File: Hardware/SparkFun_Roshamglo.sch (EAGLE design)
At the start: 41 parts, among them IC1 ATTINY84A, J1 R_Ext, J2 USBPCB, Q1 600mA/40V, U1 IR-Receiver, U3 AP2112K-3.3V

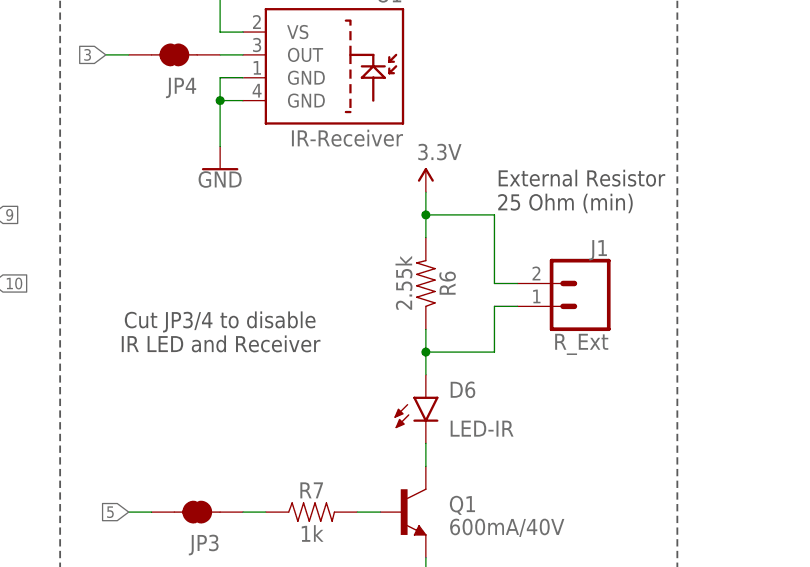
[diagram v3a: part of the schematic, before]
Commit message: v10 - replaced 2.55k resistor with 2.2k
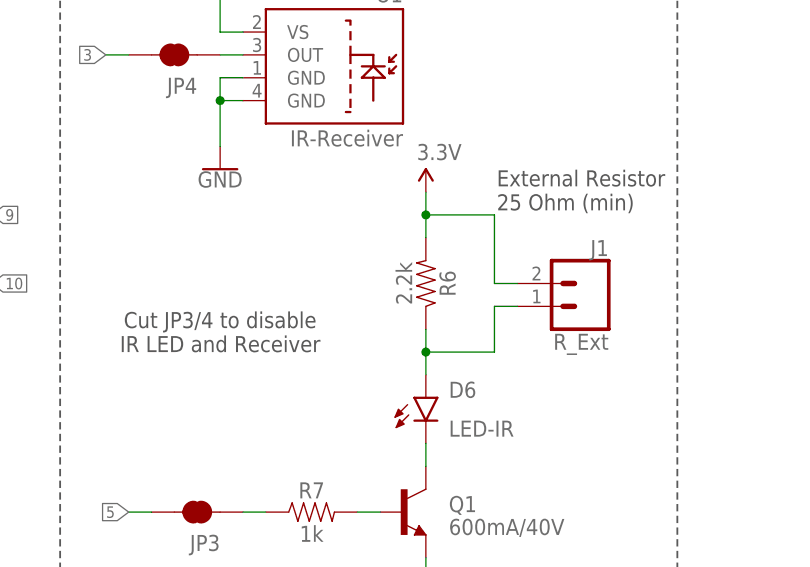
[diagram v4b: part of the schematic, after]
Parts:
- R6: value 2.55k -> 2.2k; device SparkFun-Resistors:2.55KOHM-0603-1/10W-1% -> SparkFun-Resistors:2.2KOHM-0603-1/10W-1%
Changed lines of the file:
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@@
 <grid distance="0.1" unitdist="inch" unit="inch" style="lines" multiple="1" display="no" altdistance="0.01" altunitdist="inch" altunit="inch"/>
 <layers>
-<layer number="1" name="Top" color="4" fill="1" visible="yes" active="no"/>
-<layer number="2" name="Route2" color="1" fill="3" visible="yes" active="no"/>
-<layer number="3" name="Route3" color="4" fill="3" visible="yes" active="no"/>
-<layer number="4" name="Route4" color="1" fill="4" visible="yes" active="no"/>
-<layer number="5" name="Route5" color="4" fill="4" visible="yes" active="no"/>
-<layer number="6" name="Route6" color="1" fill="8" visible="yes" active="no"/>
-<layer number="7" name="Route7" color="4" fill="8" visible="yes" active="no"/>
-<layer number="8" name="Route8" color="1" fill="2" visible="yes" active="no"/>
-<layer number="9" name="Route9" color="4" fill="2" visible="yes" active="no"/>
-<layer number="10" name="Route10" color="1" fill="7" visible="yes" active="no"/>
-<layer number="11" name="Route11" color="4" fill="7" visible="yes" active="no"/>
-<layer number="12" name="Route12" color="1" fill="5" visible="yes" active="no"/>
-<layer number="13" name="Route13" color="4" fill="5" visible="yes" active="no"/>
-<layer number="14" name="Route14" color="1" fill="6" visible="yes" active="no"/>
-<layer number="15" name="Route15" color="4" fill="6" visible="yes" active="no"/>
-<layer number="16" name="Bottom" color="1" fill="1" visible="yes" active="no"/>
-<layer number="17" name="Pads" color="2" fill="1" visible="yes" active="no"/>
-<layer number="18" name="Vias" color="2" fill="1" visible="yes" active="no"/>
-<layer number="19" name="Unrouted" color="6" fill="1" visible="yes" active="no"/>
-<layer number="20" name="Dimension" color="15" fill="1" visible="yes" active="no"/>
-<layer number="21" name="tPlace" color="16" fill="1" visible="yes" active="no"/>
-<layer number="22" name="bPlace" color="14" fill="1" visible="yes" active="no"/>
-<layer number="23" name="tOrigins" color="15" fill="1" visible="yes" active="no"/>
-<layer number="24" name="bOrigins" color="15" fill="1" visible="yes" active="no"/>
-<layer number="25" name="tNames" color="7" fill="1" visible="yes" active="no"/>
-<layer number="26" name="bNames" color="7" fill="1" visible="yes" active="no"/>
-<layer number="27" name="tValues" color="7" fill="1" visible="yes" active="no"/>
-<layer number="28" name="bValues" color="7" fill="1" visible="yes" active="no"/>
+<layer number="1" name="Top" color="4" fill="1" visible="no" active="no"/>
+<layer number="2" name="Route2" color="1" fill="3" visible="no" active="no"/>
+<layer number="3" name="Route3" color="4" fill="3" visible="no" active="no"/>
+<layer number="4" name="Route4" color="1" fill="4" visible="no" active="no"/>
+<layer number="5" name="Route5" color="4" fill="4" visible="no" active="no"/>
+<layer number="6" name="Route6" color="1" fill="8" visible="no" active="no"/>
+<layer number="7" name="Route7" color="4" fill="8" visible="no" active="no"/>
+<layer number="8" name="Route8" color="1" fill="2" visible="no" active="no"/>
+<layer number="9" name="Route9" color="4" fill="2" visible="no" active="no"/>
+<layer number="10" name="Route10" color="1" fill="7" visible="no" active="no"/>
+<layer number="11" name="Route11" color="4" fill="7" visible="no" active="no"/>
+<layer number="12" name="Route12" color="1" fill="5" visible="no" active="no"/>
+<layer number="13" name="Route13" color="4" fill="5" visible="no" active="no"/>
+<layer number="14" name="Route14" color="1" fill="6" visible="no" active="no"/>
+<layer number="15" name="Route15" color="4" fill="6" visible="no" active="no"/>
+<layer number="16" name="Bottom" color="1" fill="1" visible="no" active="no"/>
+<layer number="17" name="Pads" color="2" fill="1" visible="no" active="no"/>
+<layer number="18" name="Vias" color="2" fill="1" visible="no" active="no"/>
+<layer number="19" name="Unrouted" color="6" fill="1" visible="no" active="no"/>
+<layer number="20" name="Dimension" color="15" fill="1" visible="no" active="no"/>
+<layer number="21" name="tPlace" color="16" fill="1" visible="no" active="no"/>
+<layer number="22" name="bPlace" color="14" fill="1" visible="no" active="no"/>
+<layer number="23" name="tOrigins" color="15" fill="1" visible="no" active="no"/>
+<layer number="24" name="bOrigins" color="15" fill="1" visible="no" active="no"/>
+<layer number="25" name="tNames" color="7" fill="1" visible="no" active="no"/>
+<layer number="26" name="bNames" color="7" fill="1" visible="no" active="no"/>
+<layer number="27" name="tValues" color="7" fill="1" visible="no" active="no"/>
+<layer number="28" name="bValues" color="7" fill="1" visible="no" active="no"/>
 <layer number="29" name="tStop" color="7" fill="3" visible="no" active="no"/>
 <layer number="30" name="bStop" color="7" fill="6" visible="no" active="no"/>
@@
 <layer number="35" name="tGlue" color="7" fill="4" visible="no" active="no"/>
 <layer number="36" name="bGlue" color="7" fill="5" visible="no" active="no"/>
-<layer number="37" name="tTest" color="7" fill="1" visible="yes" active="no"/>
-<layer number="38" name="bTest" color="7" fill="1" visible="yes" active="no"/>
+<layer number="37" name="tTest" color="7" fill="1" visible="no" active="no"/>
+<layer number="38" name="bTest" color="7" fill="1" visible="no" active="no"/>
 <layer number="39" name="tKeepout" color="4" fill="11" visible="no" active="no"/>
 <layer number="40" name="bKeepout" color="1" fill="11" visible="no" active="no"/>
@@
 <layer number="44" name="Drills" color="7" fill="1" visible="no" active="no"/>
 <layer number="45" name="Holes" color="7" fill="1" visible="no" active="no"/>
-<layer number="46" name="Milling" color="3" fill="1" visible="yes" active="no"/>
-<layer number="47" name="Measures" color="7" fill="1" visible="yes" active="no"/>
-<layer number="48" name="Document" color="7" fill="1" visible="yes" active="no"/>
-<layer number="49" name="Reference" color="7" fill="1" visible="yes" active="no"/>
-<layer number="50" name="dxf" color="7" fill="1" visible="yes" active="no"/>
-<layer number="51" name="tDocu" color="6" fill="1" visible="yes" active="no"/>
-<layer number="52" name="bDocu" color="7" fill="1" visible="yes" active="no"/>
-<layer number="53" name="tGND_GNDA" color="7" fill="9" visible="yes" active="no"/>
-<layer number="54" name="bGND_GNDA" color="1" fill="9" visible="yes" active="no"/>
-<layer number="56" name="wert" color="7" fill="1" visible="yes" active="no"/>
-<layer number="57" name="tCAD" color="7" fill="1" visible="yes" active="no"/>
-<layer number="59" name="tCarbon" color="7" fill="1" visible="yes" active="no"/>
-<layer number="60" name="bCarbon" color="7" fill="1" visible="yes" active="no"/>
+<layer number="46" name="Milling" color="3" fill="1" visible="no" active="no"/>
+<layer number="47" name="Measures" color="7" fill="1" visible="no" active="no"/>
+<layer number="48" name="Document" color="7" fill="1" visible="no" active="no"/>
+<layer number="49" name="Reference" color="7" fill="1" visible="no" active="no"/>
+<layer number="50" name="dxf" color="7" fill="1" visible="no" active="no"/>
+<layer number="51" name="tDocu" color="6" fill="1" visible="no" active="no"/>
+<layer number="52" name="bDocu" color="7" fill="1" visible="no" active="no"/>
+<layer number="53" name="tGND_GNDA" color="7" fill="9" visible="no" active="no"/>
+<layer number="54" name="bGND_GNDA" color="1" fill="9" visible="no" active="no"/>
+<layer number="56" name="wert" color="7" fill="1" visible="no" active="no"/>
+<layer number="57" name="tCAD" color="7" fill="1" visible="no" active="no"/>
+<layer number="59" name="tCarbon" color="7" fill="1" visible="no" active="no"/>
+<layer number="60" name="bCarbon" color="7" fill="1" visible="no" active="no"/>
 <layer number="90" name="Modules" color="5" fill="1" visible="yes" active="yes"/>
 <layer number="91" name="Nets" color="2" fill="1" visible="yes" active="yes"/>
@@
 <part name="SUPPLY9" library="SparkFun-Aesthetics" deviceset="3.3V" device=""/>
 <part name="SUPPLY13" library="SparkFun-PowerSymbols" deviceset="VIN" device=""/>
-<part name="R6" library="SparkFun-Resistors" deviceset="2.55KOHM" device="-0603-1/10W-1%" value="2.55k"/>
+<part name="R6" library="SparkFun-Resistors" deviceset="2.2KOHM" device="-0603-1/10W-1%" value="2.2k"/>
 <part name="FD1" library="SparkFun-Aesthetics" deviceset="FIDUCIAL" device="UFIDUCIAL"/>
 <part name="FD2" library="SparkFun-Aesthetics" deviceset="FIDUCIAL" device="UFIDUCIAL"/>

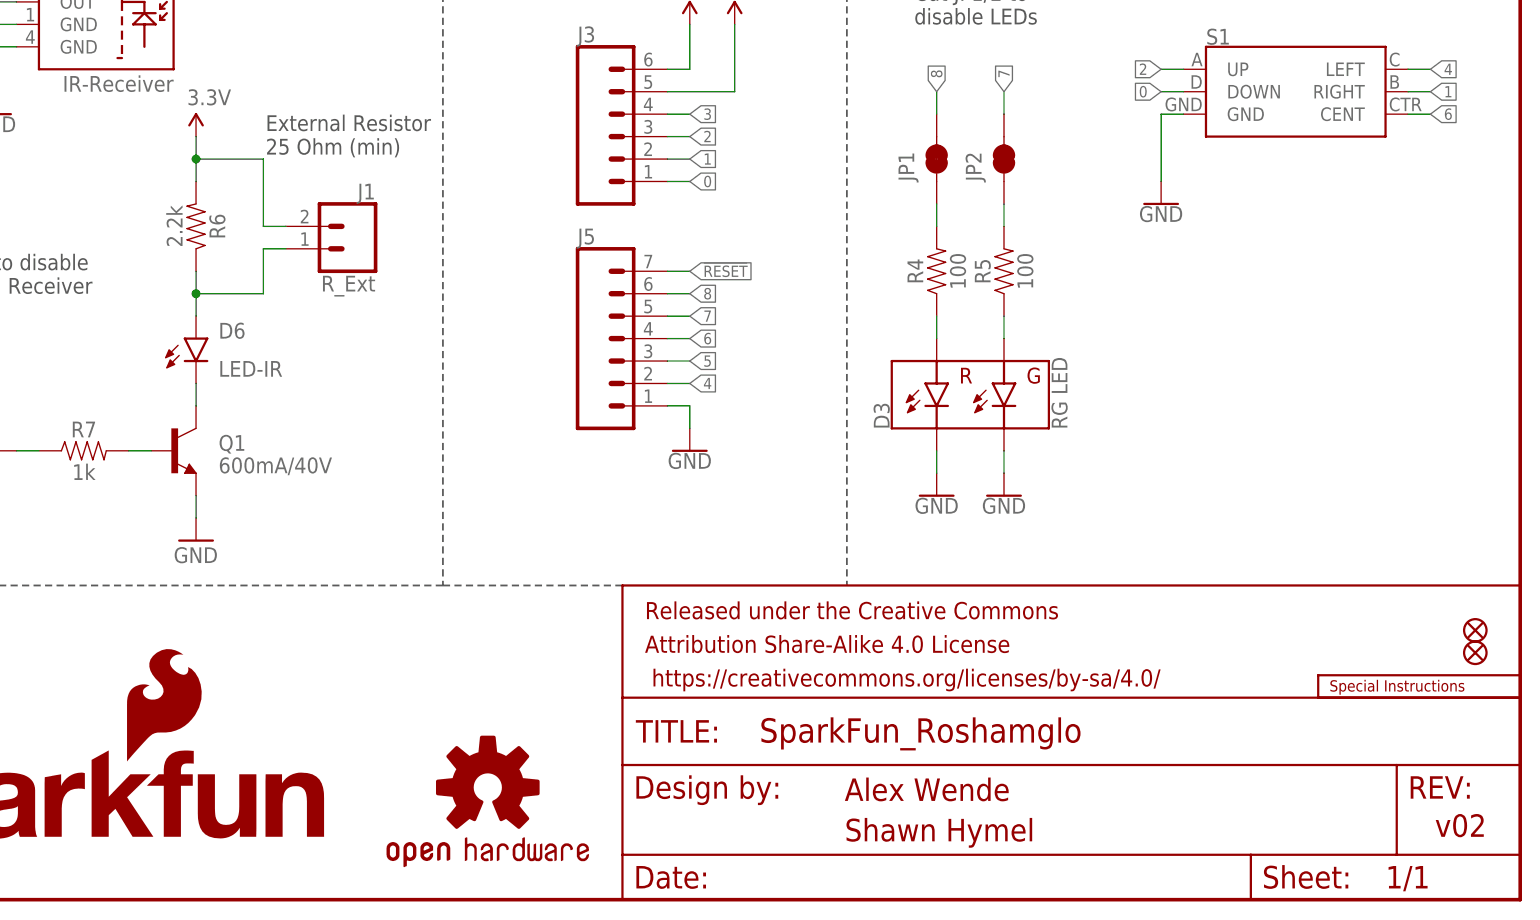
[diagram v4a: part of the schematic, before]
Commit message: Design Review changes
Replaced some silk, and moved a via
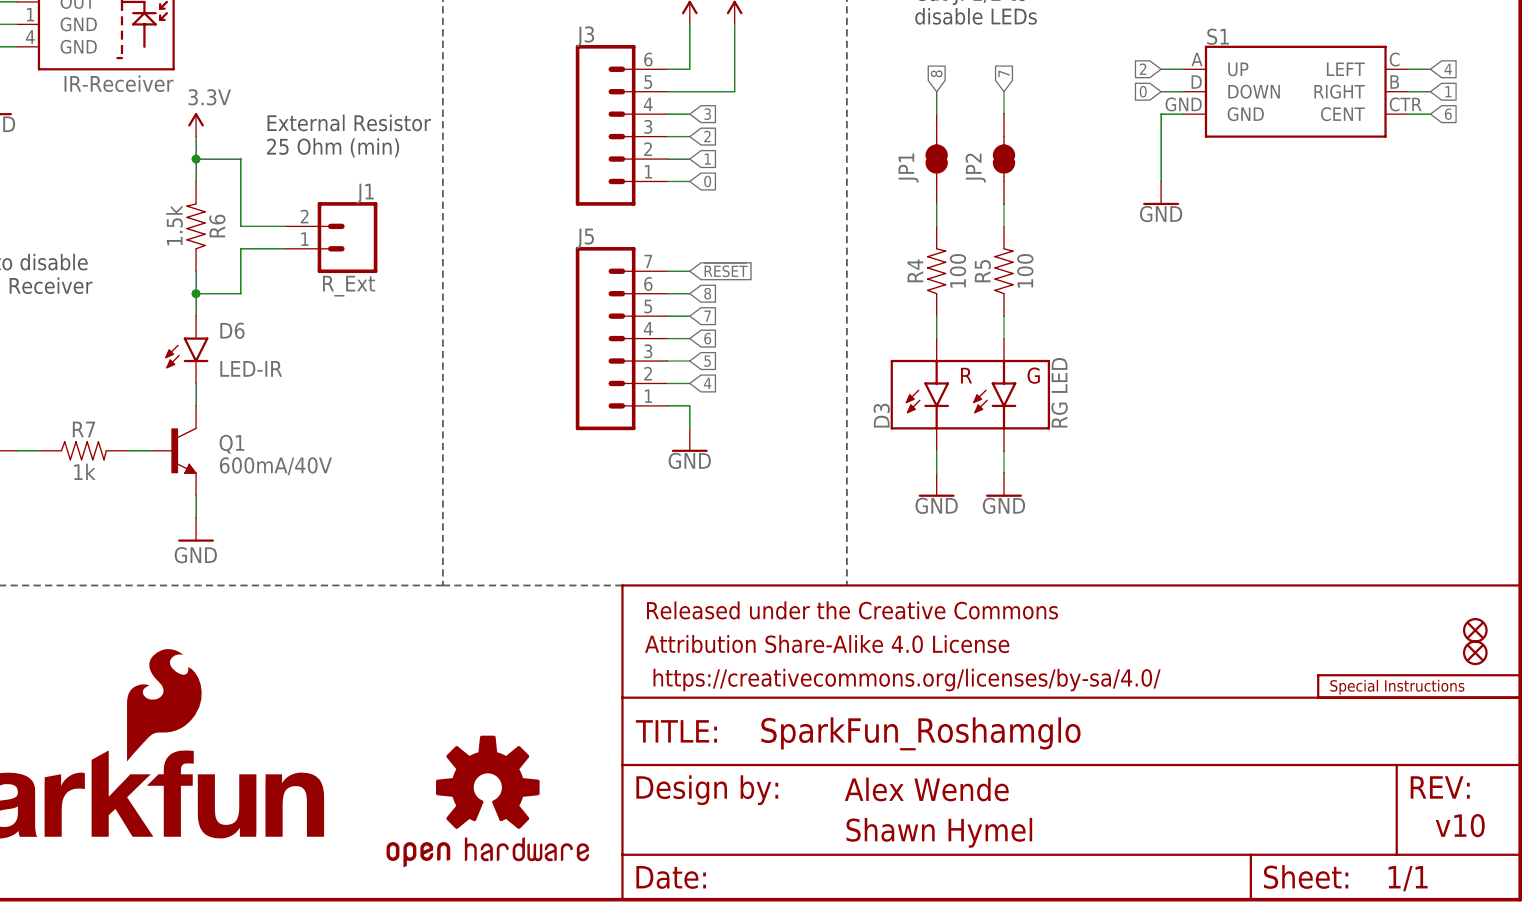
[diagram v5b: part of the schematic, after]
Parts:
- R6: value 2.2k -> 1.5k; device SparkFun-Resistors:2.2KOHM-0603-1/10W-1% -> SparkFun-Resistors:1.5KOHM-0603-1/10W-1%
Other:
- note added: "v10"
- note removed: "v02"
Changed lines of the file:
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@@
 <part name="SUPPLY9" library="SparkFun-Aesthetics" deviceset="3.3V" device=""/>
 <part name="SUPPLY13" library="SparkFun-PowerSymbols" deviceset="VIN" device=""/>
-<part name="R6" library="SparkFun-Resistors" deviceset="2.2KOHM" device="-0603-1/10W-1%" value="2.2k"/>
+<part name="R6" library="SparkFun-Resistors" deviceset="1.5KOHM" device="-0603-1/10W-1%" value="1.5k"/>
 <part name="FD1" library="SparkFun-Aesthetics" deviceset="FIDUCIAL" device="UFIDUCIAL"/>
 <part name="FD2" library="SparkFun-Aesthetics" deviceset="FIDUCIAL" device="UFIDUCIAL"/>
@@
 <text x="172.466" y="11.176" size="2.54" layer="94">Alex Wende</text>
 <text x="172.466" y="6.604" size="2.54" layer="94">Shawn Hymel</text>
-<text x="239.268" y="7.112" size="2.54" layer="94">v02</text>
+<text x="239.268" y="7.112" size="2.54" layer="94">v10</text>
 <text x="129.54" y="116.84" size="2.54" layer="94">IO Breakout</text>
 <wire x1="127" y1="121.92" x2="127" y2="35.56" width="0.2032" layer="97" style="shortdash"/>
@@
 <wire x1="99.06" y1="81.28" x2="99.06" y2="83.82" width="0.1524" layer="91"/>
 <wire x1="99.06" y1="83.82" x2="99.06" y2="86.36" width="0.1524" layer="91"/>
-<wire x1="106.68" y1="76.2" x2="106.68" y2="83.82" width="0.1524" layer="91"/>
-<wire x1="106.68" y1="83.82" x2="99.06" y2="83.82" width="0.1524" layer="91"/>
+<wire x1="104.14" y1="76.2" x2="104.14" y2="83.82" width="0.1524" layer="91"/>
+<wire x1="104.14" y1="83.82" x2="99.06" y2="83.82" width="0.1524" layer="91"/>
 <junction x="99.06" y="83.82"/>
 <pinref part="J1" gate="G$1" pin="2"/>
-<wire x1="109.22" y1="76.2" x2="106.68" y2="76.2" width="0.1524" layer="91"/>
+<wire x1="109.22" y1="76.2" x2="104.14" y2="76.2" width="0.1524" layer="91"/>
 </segment>
 <segment>
@@
 <net name="N$14" class="0">
 <segment>
-<wire x1="106.68" y1="73.66" x2="106.68" y2="68.58" width="0.1524" layer="91"/>
+<wire x1="104.14" y1="73.66" x2="104.14" y2="68.58" width="0.1524" layer="91"/>
 <pinref part="R6" gate="G$1" pin="1"/>
 <pinref part="D6" gate="G$1" pin="A"/>
 <wire x1="99.06" y1="71.12" x2="99.06" y2="68.58" width="0.1524" layer="91"/>
 <wire x1="99.06" y1="68.58" x2="99.06" y2="66.04" width="0.1524" layer="91"/>
-<wire x1="106.68" y1="68.58" x2="99.06" y2="68.58" width="0.1524" layer="91"/>
+<wire x1="104.14" y1="68.58" x2="99.06" y2="68.58" width="0.1524" layer="91"/>
 <junction x="99.06" y="68.58"/>
 <pinref part="J1" gate="G$1" pin="1"/>
-<wire x1="106.68" y1="73.66" x2="109.22" y2="73.66" width="0.1524" layer="91"/>
-</segment>
-</net>
+<wire x1="104.14" y1="73.66" x2="109.22" y2="73.66" width="0.1524" layer="91"/>
+</segment>
+</net>
